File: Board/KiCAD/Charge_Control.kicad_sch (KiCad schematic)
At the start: 51 parts, among them Q1 AON7408, Q10 AON7407, Q2 AON6500, Q3 AON7408, Q4 AON6500, U1 BQ25730RSNR

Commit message: Add files via upload
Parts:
- added R76: 50m, symbol Device:R_Small
- added U3: LTC2943CDD_PBF, Package_SO:SOIC-8-1EP_3.9x4.9mm_P1.27mm_EP2.29x3mm, symbol LTC2943CDD_PBF:LTC2943CDD_PBF
- C40: value C -> 1uF
- R7, R8: value R -> 350k
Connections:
- net BATT: now also R76.1, U3.8 (SENSE-); no longer C23.2, C25.1, R4.2, R6.2
- net GND: now also U3.2 (GND), U3.3 (GND), U3.7 (GND), U3.9 (EXP)
- net SCL: now also U3.4 (SCL)
- net SDA: now also U3.5 (SDA)
- new net: C23.2, C25.1, R4.2, R6.2, R76.2, U3.1 (SENSE+)
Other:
- note added: "Vsys: The voltage being delivered to an external Voltage/Amperage: User Dependent"
- note removed: "Power Host from Vin or Vbatt Voltage range? Current range?"
- moved on the sheet: C10, C12, C13, C14, C15, C22, C23, C24, C25, C26, C27, C35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

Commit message: Add files via upload
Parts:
- removed R11, R12, R16: R, symbol Device:R_Small
- added C28, C29: 10uF, Capacitor_SMD:C_0201_0603Metric, symbol Device:C_Small
- added C45: 33uF, Capacitor_SMD:C_0201_0603Metric, symbol Device:C_Small
- C10, C12, C22, C25: value C -> 10uF; footprint (none) -> Capacitor_SMD:C_0201_0603Metric
- C13: value C -> 1uF; footprint (none) -> Capacitor_SMD:C_0201_0603Metric
- C14, C15: value C -> 47nF; footprint (none) -> Capacitor_SMD:C_0201_0603Metric
- C23, C24: value C -> 0.1uF; footprint (none) -> Capacitor_SMD:C_0201_0603Metric
- C26: value C -> 3.3uF; footprint (none) -> Capacitor_SMD:C_0201_0603Metric
- C27, C35: value C -> 100pF; footprint (none) -> Capacitor_SMD:C_0201_0603Metric
- C36: value C -> 33pF; footprint (none) -> Capacitor_SMD:C_0201_0603Metric
- C37: value C -> 15pF; footprint (none) -> Capacitor_SMD:C_0201_0603Metric
- C38: value C -> 4.7nF; footprint (none) -> Capacitor_SMD:C_0201_0603Metric
- C39: value C -> 680pF; footprint (none) -> Capacitor_SMD:C_0201_0603Metric
- C40: footprint (none) -> Capacitor_SMD:C_0201_0603Metric
- C41, C9: value C -> 10nF; footprint (none) -> Capacitor_SMD:C_0201_0603Metric
- C42, C43: value C -> 33nF; footprint (none) -> Capacitor_SMD:C_0201_0603Metric
- C44: value C -> 33uF; footprint (none) -> Capacitor_SMD:C_0201_0603Metric
- C7: value C -> 1nF; footprint (none) -> Capacitor_SMD:C_0201_0603Metric
- L2: value L -> 4.7uH; footprint (none) -> Inductor_SMD:L_10.4x10.4_H4.8
- R10: value R -> 30k; footprint (none) -> Resistor_SMD:R_0201_0603Metric
- R15, R35: value R -> 10k; footprint (none) -> Resistor_SMD:R_0201_0603Metric
- R2, R4: value R -> 10m; footprint (none) -> Resistor_SMD:R_0201_0603Metric
- R3: value R -> 2.2m; footprint (none) -> Resistor_SMD:R_0201_0603Metric
- R36: value R -> 15k; footprint (none) -> Resistor_SMD:R_0201_0603Metric
- R37: value R -> 39k; footprint (none) -> Resistor_SMD:R_0201_0603Metric
- R38: value R -> 220k; footprint (none) -> Resistor_SMD:R_0201_0603Metric
- R39: value R -> 380k; footprint (none) -> Resistor_SMD:R_0201_0603Metric
- R40, R5, R6: value R -> 10; footprint (none) -> Resistor_SMD:R_0201_0603Metric
- R41: value R -> 5,1; footprint (none) -> Resistor_SMD:R_0201_0603Metric
- R42: value R -> 5.1; footprint (none) -> Resistor_SMD:R_0201_0603Metric
- R7, R8: footprint (none) -> Resistor_SMD:R_0201_0603Metric
- R76: footprint (none) -> Resistor_SMD:R_1206_3216Metric
- R9: value R -> 200k; footprint (none) -> Resistor_SMD:R_0201_0603Metric
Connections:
- net GND: now also U1.14 (CMPIN), C28.2, C29.2, C45.2
- net VDDA: no longer R40.1
- net Vsys: now also C29.1, C45.1
- net at C23.2, C25.1, R4.2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: now also C28.1
- net at C23.1, C24.1, R4.1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: now also Q10.1, Q10.2, Q10.3; no longer Q10.1-3
- net CMPOUT: no longer names the net of U1.15 (CMPOUT)
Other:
- note added: "To Microcontroller"
- note removed: "To uC"
- moved on the sheet: C22, C25, R42, R76, U3

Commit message: Add files via upload
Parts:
- removed C7: 1nF, Capacitor_SMD:C_0201_0603Metric, symbol Device:C_Small
- removed Q2, Q4: AON6500, AON6500:TRANS_AON6500, symbol AON6500:AON6500
- removed R40: 10, Resistor_SMD:R_0201_0603Metric, symbol Device:R_Small
- added Q2, Q4: AON7408, AON7408:TRANS_AON7408, symbol AON7408:AON7408
- C10, C12, C22, C25, C28, C29: footprint Capacitor_SMD:C_0201_0603Metric -> Capacitor_SMD:C_1206_3216Metric; MFR (none) -> SAMSUNG; MPN (none) -> CL31A106KBHNNNE
- C13, C14, C15, C23, C24, C26, C27, C35, C36, C37, C38, C39, C40, C41, C42, C43, C44, C45, C9: footprint Capacitor_SMD:C_0201_0603Metric -> Capacitor_SMD:C_0603_1608Metric
- Q10: MF Alpha & Omega Semiconductor -> (none); MFR (none) -> Alpha & Omega Semiconductor; MP AON7407 -> (none); MPN (none) -> AON7407
- R10, R15, R35, R36, R37, R38, R39, R41, R42, R5, R6, R7, R8, R9: footprint Resistor_SMD:R_0201_0603Metric -> Resistor_SMD:R_0603_1608Metric
- R2, R4: footprint Resistor_SMD:R_0201_0603Metric -> Resistor_SMD:R_1206_3216Metric
- R3: value 2.2m -> 2.2; footprint Resistor_SMD:R_0201_0603Metric -> Resistor_SMD:R_0603_1608Metric
- U1: MF Texas Instruments -> (none); MFR (none) -> Texas Instruments; MP BQ25730RSNR -> (none); MPN (none) -> BQ25730RSNR
- U3: MF Analog Devices -> (none); MFR (none) -> Analog Devices; MP LTC2943CDD#PBF -> (none); MPN (none) -> LTC2943CDD#PBF
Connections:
- net GND: now also Q2.1, Q2.2, Q2.3
- net Vsys: now also Q4.9
- net at C15.1, L2.2, Q3.9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: now also Q4.1, Q4.2, Q4.3
- net at U1.24 (HIDRV2): now also Q4.4
- net at U1.29 (LODRV1): now also Q2.4
- net at C14.1, L2.1, Q1.1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: now also Q2.9
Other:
- note added: "Power in from host 24V/4A"
- note added: "To the cells"
- note removed: "Does this need VDDA?"
- note removed: "Doesn't go off sheet, so changed to supply pin"
- note removed: "Power in from host Voltage range? Current range?"
- note removed: "To the cells Voltage range? Current range?"
- note removed: "Vsys: The voltage being delivered to an external Voltage/Amperage: User Dependent"
- moved on the sheet: C9

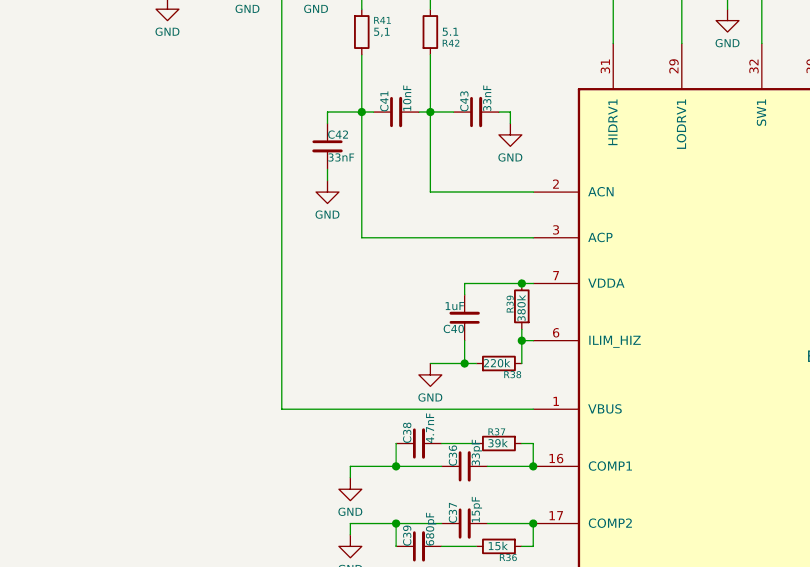
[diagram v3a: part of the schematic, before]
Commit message: Updated Schematic & PCB Layout
Updated the look of the PCB layout to make the power flow Vin more intuitive.

@KeytarGoblin
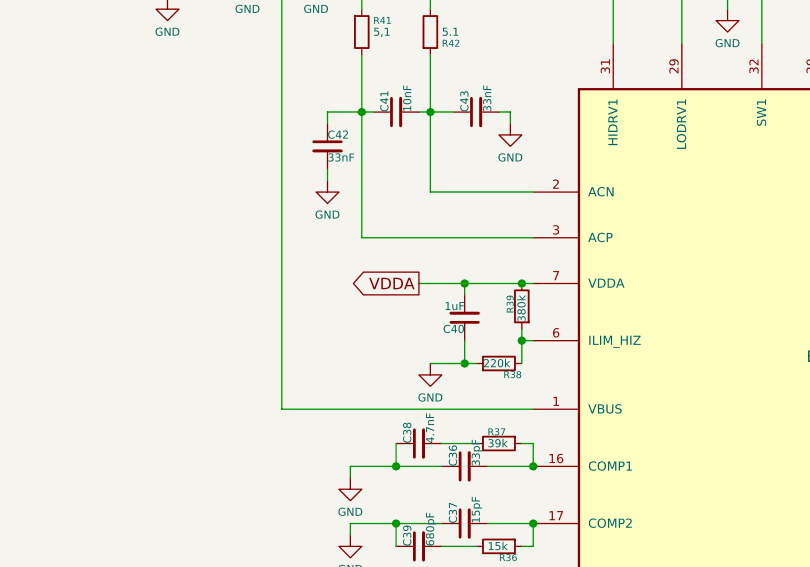
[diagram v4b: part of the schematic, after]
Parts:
- C44, C45: footprint Capacitor_SMD:C_0603_1608Metric -> Capacitor_SMD:C_1206_3216Metric
- R3, R41, R42: footprint Resistor_SMD:R_0603_1608Metric -> Resistor_SMD:R_1206_3216Metric
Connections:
- net VDDA: now also C40.2, R39.2, U1.7 (VDDA)
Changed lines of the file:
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@@
 	)
 	(junction
+		(at 78.74 81.28)
+		(diameter 0)
+		(color 0 0 0 0)
+	)
+	(junction
 		(at 58.42 35.56)
 		(diameter 0)
@@
 	(wire
 		(pts
+			(xy 73.66 81.28) (xy 78.74 81.28)
+		)
+		(stroke
+			(width 0)
+			(type default)
+		)
+	)
+	(wire
+		(pts
 			(xy 85.09 86.36) (xy 85.09 87.63)
 		)
@@
 		)
 	)
+	(global_label "VDDA"
+		(shape output)
+		(at 73.66 81.28 180)
+		(fields_autoplaced yes)
+		(effects
+			(font
+				(size 1.27 1.27)
+			)
+			(justify right)
+		)
+		(property "Intersheetrefs" "${INTERSHEET_REFS}"
+			(at 65.9576 81.28 0)
+			(effects
+				(font
+					(size 1.27 1.27)
+				)
+				(justify right)
+				(hide yes)
+			)
+		)
+	)
 	(hierarchical_label "BATT"
 		(shape output)
@@
 			)
 		)
-		(property "Footprint" "Resistor_SMD:R_0603_1608Metric"
+		(property "Footprint" "Resistor_SMD:R_1206_3216Metric"
 			(at 74.93 53.34 0)
 			(effects
@@
 			)
 		)
-		(property "Footprint" "Resistor_SMD:R_0603_1608Metric"
+		(property "Footprint" "Resistor_SMD:R_1206_3216Metric"
 			(at 67.31 53.34 0)
 			(effects
@@
 			)
 		)
-		(property "Footprint" "Resistor_SMD:R_0603_1608Metric"
+		(property "Footprint" "Resistor_SMD:R_1206_3216Metric"
 			(at 45.72 39.37 0)
 			(effects
@@
 			)
 		)
-		(property "Footprint" "Capacitor_SMD:C_0603_1608Metric"
+		(property "Footprint" "Capacitor_SMD:C_1206_3216Metric"
 			(at 199.39 22.86 0)
 			(effects
@@
 			)
 		)
-		(property "Footprint" "Capacitor_SMD:C_0603_1608Metric"
+		(property "Footprint" "Capacitor_SMD:C_1206_3216Metric"
 			(at 194.31 22.86 0)
 			(effects

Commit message: updated version of PCB
here's my latest update @KeytarGoblin  @andrewgreenberg
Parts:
- R76: value 50m -> 20m
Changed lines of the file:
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@@
 			)
 		)
-		(property "Value" "50m"
+		(property "Value" "20m"
 			(at 213.36 43.18 90)
 			(effects

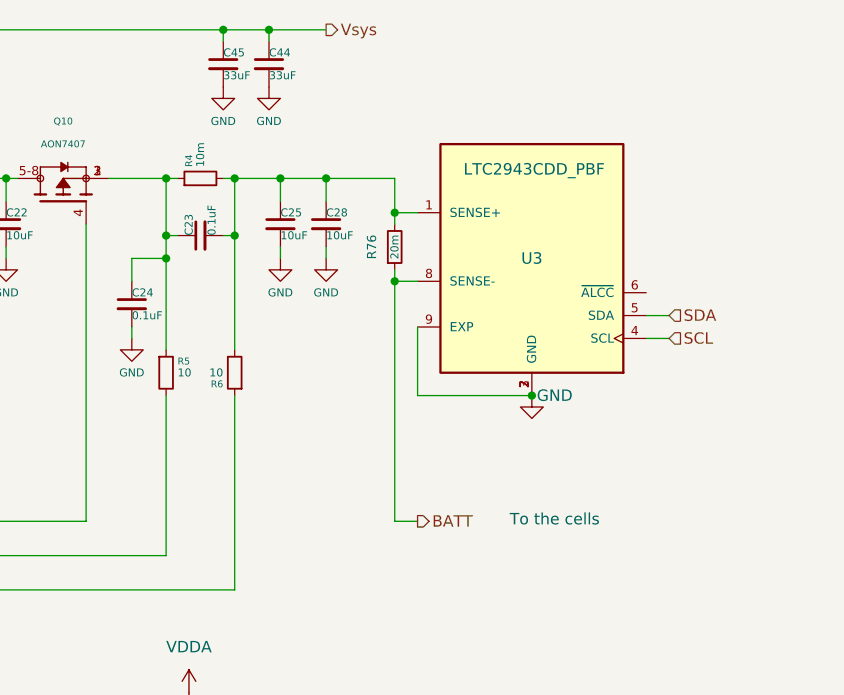
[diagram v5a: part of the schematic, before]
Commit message: Schematic: - Fixed FDI plug - Added thermistor connectors - Added a bunch of NCs using KiCAD NC tool - Added filter cap back into battery current shunt - Added bypass cap to LTC - Removed Cell 4 INA260 because the LTC does current, voltage of that top cell! Board Layout: - Chewed out team for not reading the BQ's datasheet, specifically Section 11 - Relayed out power stream using Section 11 as a refernce - Changed some footprints, mostly reducing size to 0603 - Positioned things optimally given what I thought made sense (dangerous, I know) - Fixed ground planes Other: - Removed PRL and CACHE files from the repo.
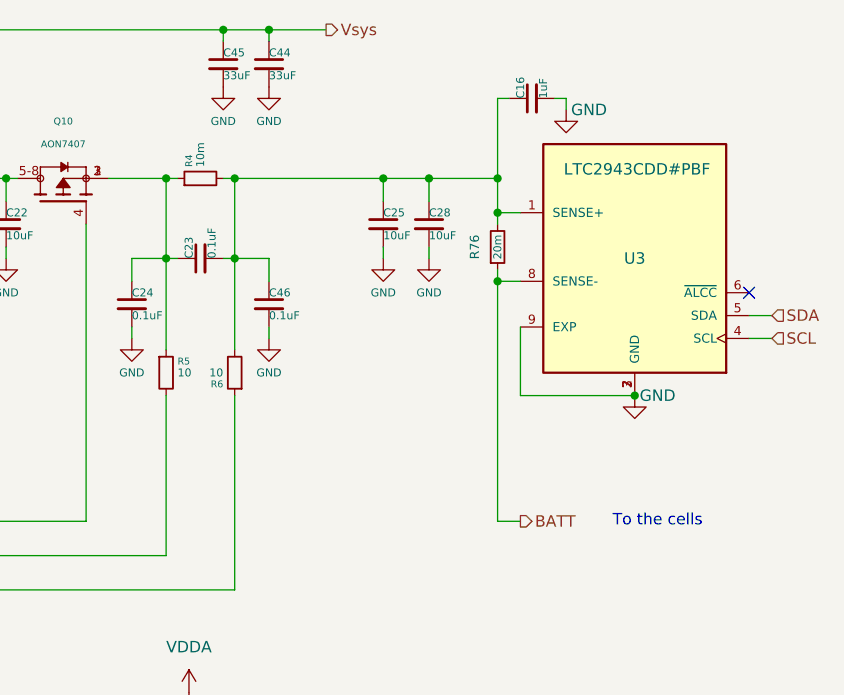
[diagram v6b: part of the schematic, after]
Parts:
- added C16: 1uF, Capacitor_SMD:C_0603_1608Metric, symbol Device:C_Small
- added C46: 0.1uF, Capacitor_SMD:C_0603_1608Metric, symbol Device:C_Small
- R41, R42: footprint Resistor_SMD:R_1206_3216Metric -> Resistor_SMD:R_0603_1608Metric
- U1: Availability In Stock -> (none); Check_prices https://www.snapeda.com/parts/BQ25730RSNR/Texas+Instruments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 -> (none); Description_1 I²C 1-5 cell NVDC buck-boost battery charge controller with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 -> (none); MANUFACTURER Texas Instruments -> (none); MAXIMUM_PACKAGE_HEIGHT 0.8 mm -> (none); PARTREV February 2021 -> (none); Package QFN-32 Texas Instruments -> (none); Price None -> (none); SNAPEDA_PN BQ25730RSNR -> (none); STANDARD Manufacturer Recommendations -> (none); SnapEDA_Link https://www.snapeda.com/parts/BQ25730RSNR/Texas+Instruments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 -> (none)
- U3: value LTC2943CDD_PBF -> LTC2943CDD#PBF; Availability In Stock -> (none); Check_prices https://www.snapeda.com/parts/LTC2943CDD%23PBF/Analog+Devic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 -> (none); Description_1 Multicell Battery Gas Gauge with Temperature, Voltage and C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 -> (none); MANUFACTURER Analog Devices -> (none); MAXIMUM_PACKAGE_HEIGHT 0.80 -> (none); PARTREV N/A -> (none); Package DFN-8 Analog Devices -> (none); Price None -> (none); STANDARD IPC 7351B -> (none); SnapEDA_Link https://www.snapeda.com/parts/LTC2943CDD%23PBF/Analog+Devic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 -> (none)
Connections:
- net GND: now also C16.2, C46.2
- net at C23.2, C25.1, C28.1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: now also C16.1, C46.1
- no-connect marks 0 -> 1
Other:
- moved on the sheet: C23, C25, C28, R76, U3

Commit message: finished PCB
PCB completed @andrewgreenberg
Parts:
- added JP1: Jumper_2_Bridged, TestPoint:TestPoint_2Pads_Pitch2.54mm_Drill0.8mm, symbol Jumper:Jumper_2_Bridged
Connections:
- net at C16.1, C23.2, C25.1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: now also JP1.1 (A); no longer R76.2, U3.1 (SENSE+)
- new net: JP1.2 (B), R76.2, U3.1 (SENSE+)
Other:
- moved on the sheet: C16, R76, U3

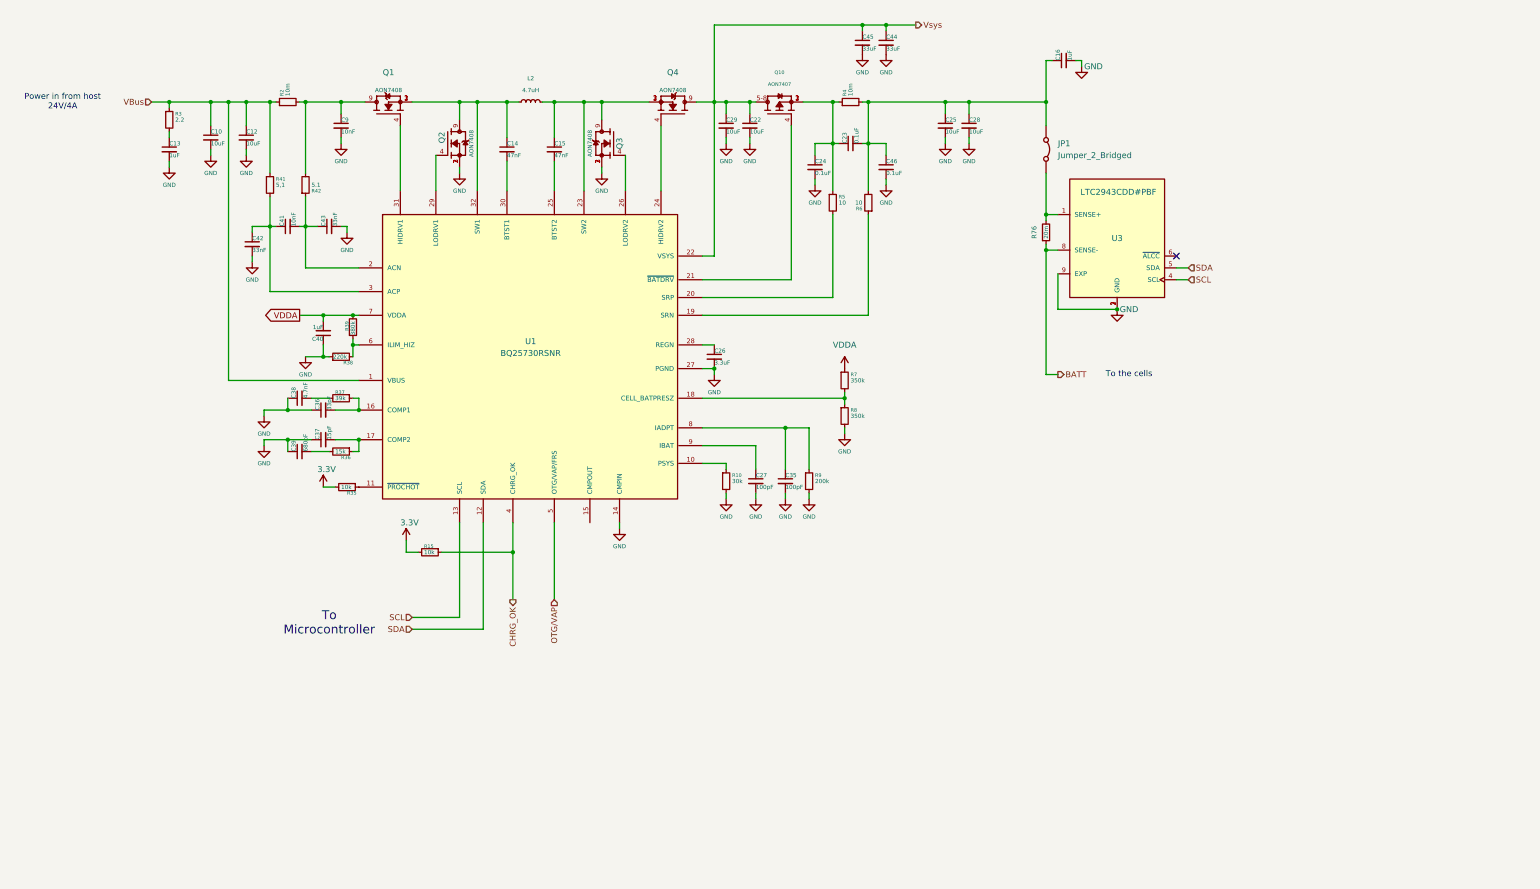
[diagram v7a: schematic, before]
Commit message: revised PCB
This design accounts for majority of the updates requested by Faculty Advisor

@KeytarGoblin  @andrewgreenberg
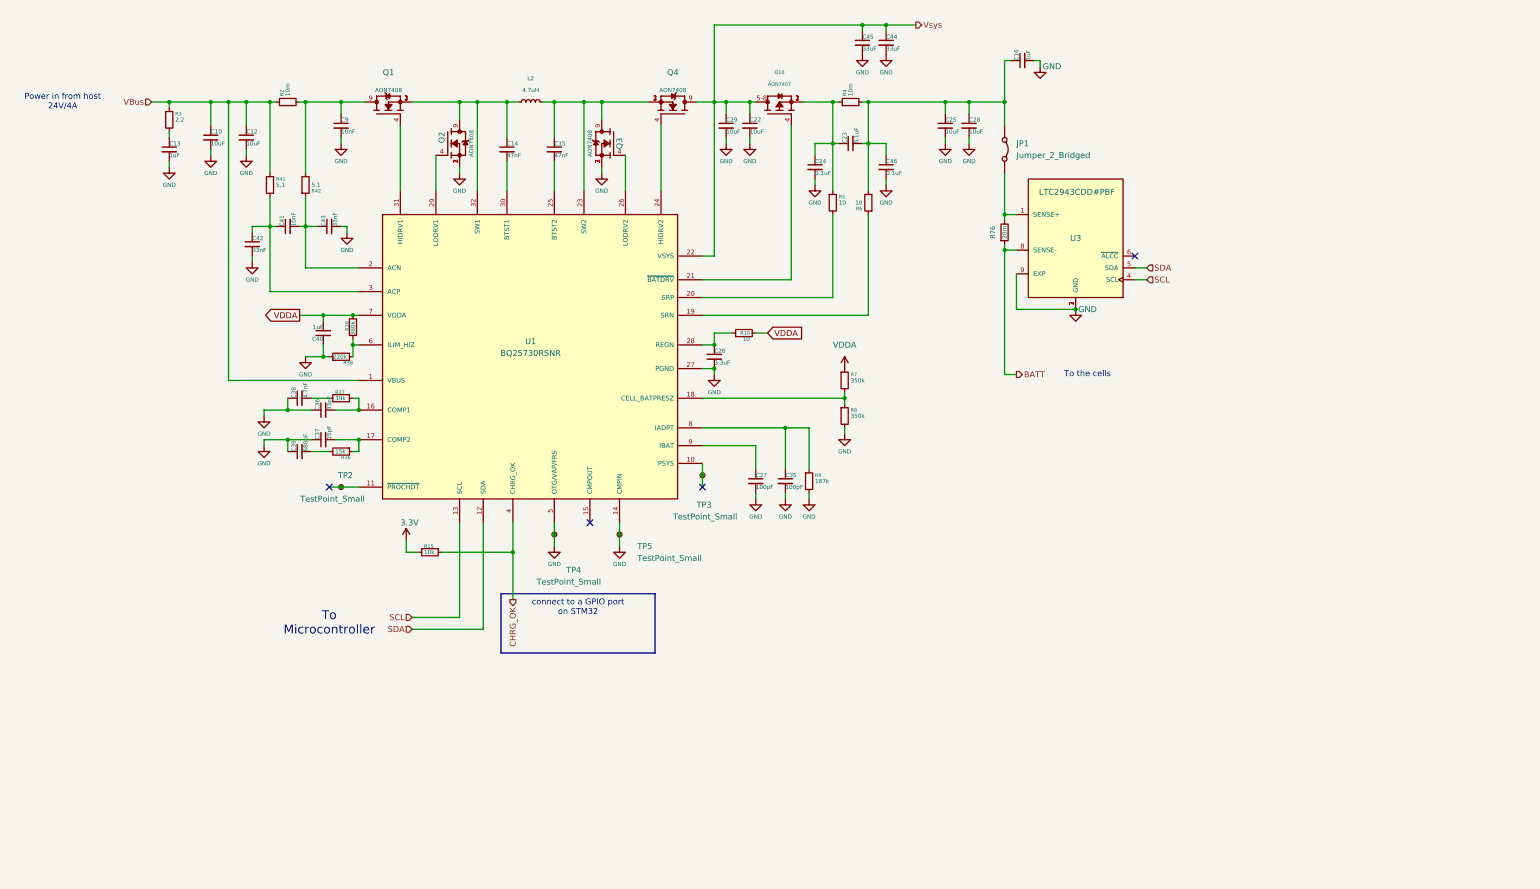
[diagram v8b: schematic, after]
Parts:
- removed R35: 10k, Resistor_SMD:R_0603_1608Metric, symbol Device:R_Small
- added TP2, TP3, TP4, TP5: TestPoint_Small, symbol Connector:TestPoint_Small
- R10: value 30k -> 10
- R9: value 200k -> 187k
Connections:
- net OTG/VAP is gone; now on net GND: U1.5 (OTG/VAP/FRS)
- net GND: now also TP4.1, TP5.1; no longer R10.2
- net VDDA: now also R10.2
- net at U1.10 (PSYS): now also TP3.1; no longer R10.1
- net at U1.11 (~{PROCHOT}): now also TP2.1
- net at C26.1, U1.28 (REGN): now also R10.1
- no-connect marks 1 -> 4
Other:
- moved on the sheet: C16, JP1, R76, U3
